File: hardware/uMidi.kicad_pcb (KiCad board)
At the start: 2 copper layers, 66 x 40.6 mm, 65 parts, among them CON1 USB-MINI-B, IC1 ATXMEGA128A4U-M, IC2 74LS14, IC3 LT1129CST-3.3, IC4 6N138, P1 MIDI In, P2 MIDI Thru, P3 MIDI T/O, P4 MIDI Out, P5 5..12 V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

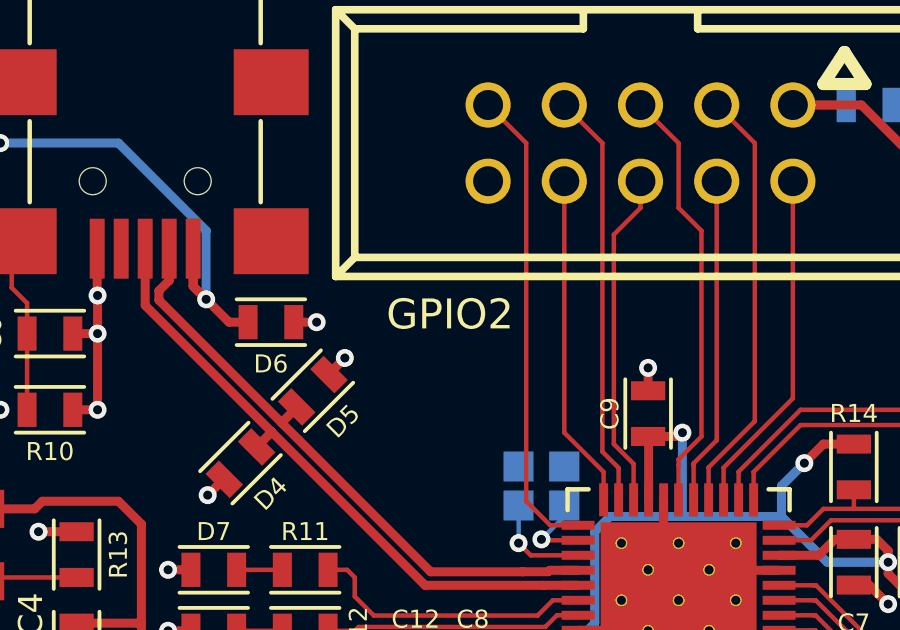
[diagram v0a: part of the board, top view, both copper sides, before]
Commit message: Fix GPIO3 value and silkscreen text
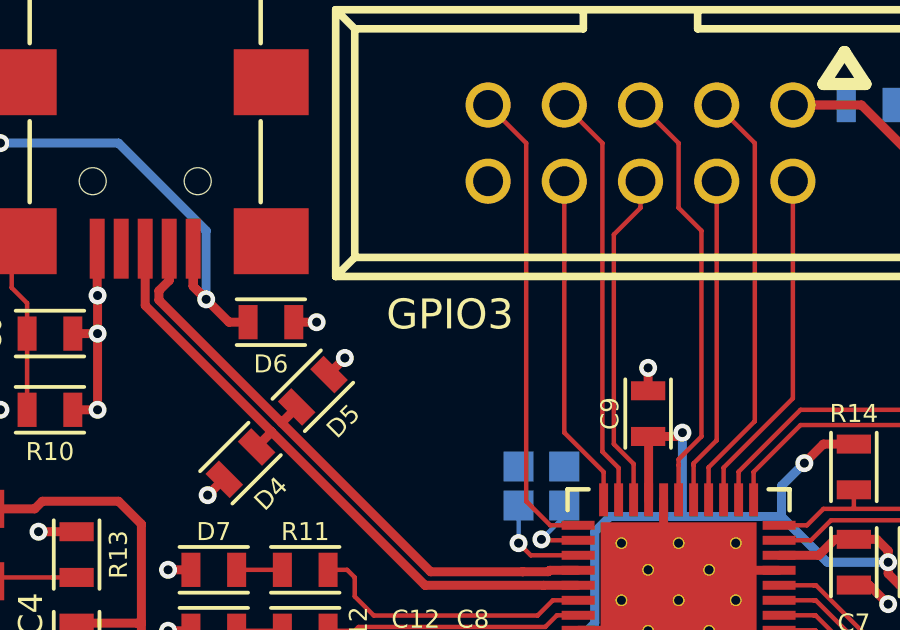
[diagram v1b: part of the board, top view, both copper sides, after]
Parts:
- P9: value GPIO2 -> GPIO3
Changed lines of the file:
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@@
     (links 166)
     (no_connects 0)
-    (area 67.259999 117.955 133.400001 166.2406)
+    (area 67.259999 123.139999 133.400001 163.880001)
     (thickness 1.6)
     (drawings 24)
@@
   (layers
     (0 F.Cu signal)
-    (31 B.Cu signal hide)
+    (31 B.Cu signal)
     (32 B.Adhes user)
     (33 F.Adhes user)
@@
       (linewidth 0.020000)
       (plotframeref false)
-      (viasonmask false)
+      (viasonmask true)
       (mode 1)
       (useauxorigin false)
@@
       (padsonsilk false)
       (subtractmaskfromsilk false)
-      (outputformat 4)
+      (outputformat 1)
       (mirror false)
-      (drillshape 2)
+      (drillshape 0)
       (scaleselection 1)
       (outputdirectory plots/))
@@
       (effects (font (size 1.778 1.778) (thickness 0.0889)))
     )
-    (fp_text value GPIO2 (at 6.35 -5.715 180) (layer F.SilkS)
+    (fp_text value GPIO3 (at 6.35 -5.715 180) (layer F.SilkS)
       (effects (font (size 1 1) (thickness 0.2)))
     )

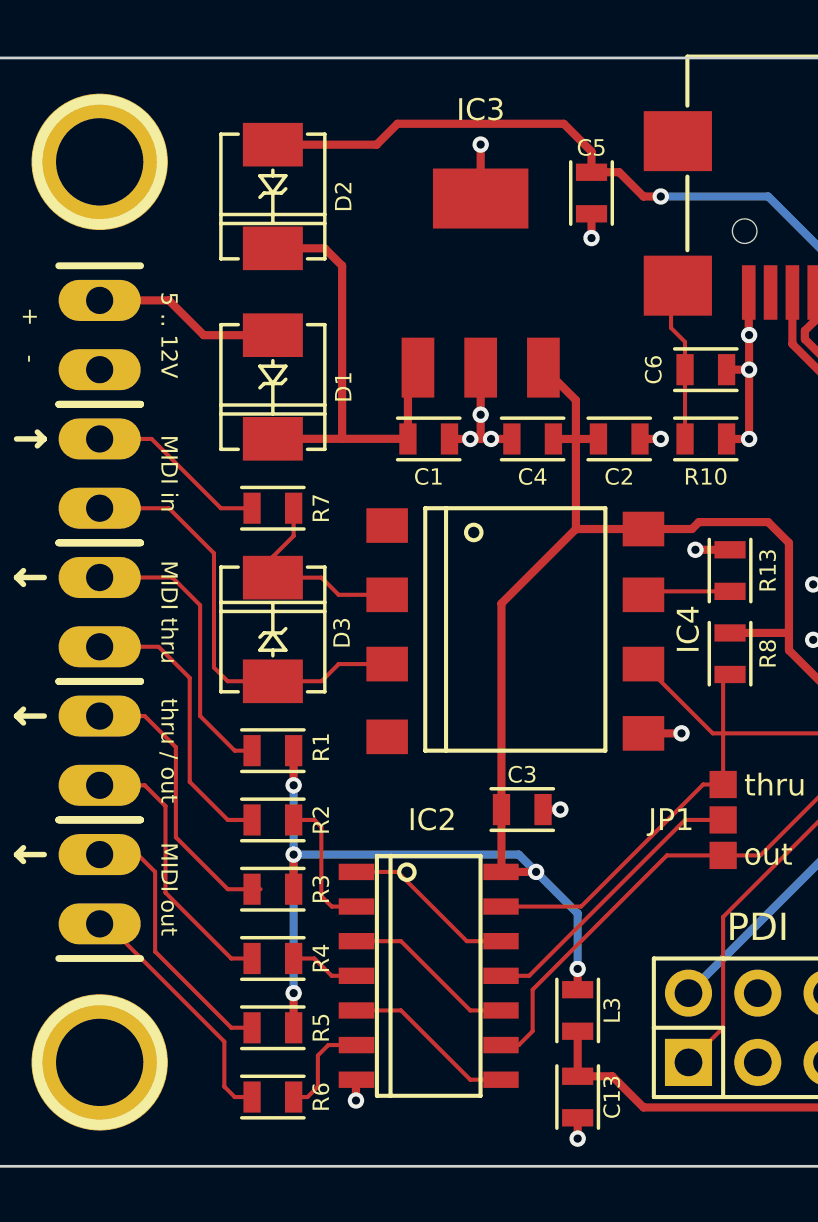
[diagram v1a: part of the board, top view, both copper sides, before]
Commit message: Revise silkscreen; Customize diode module
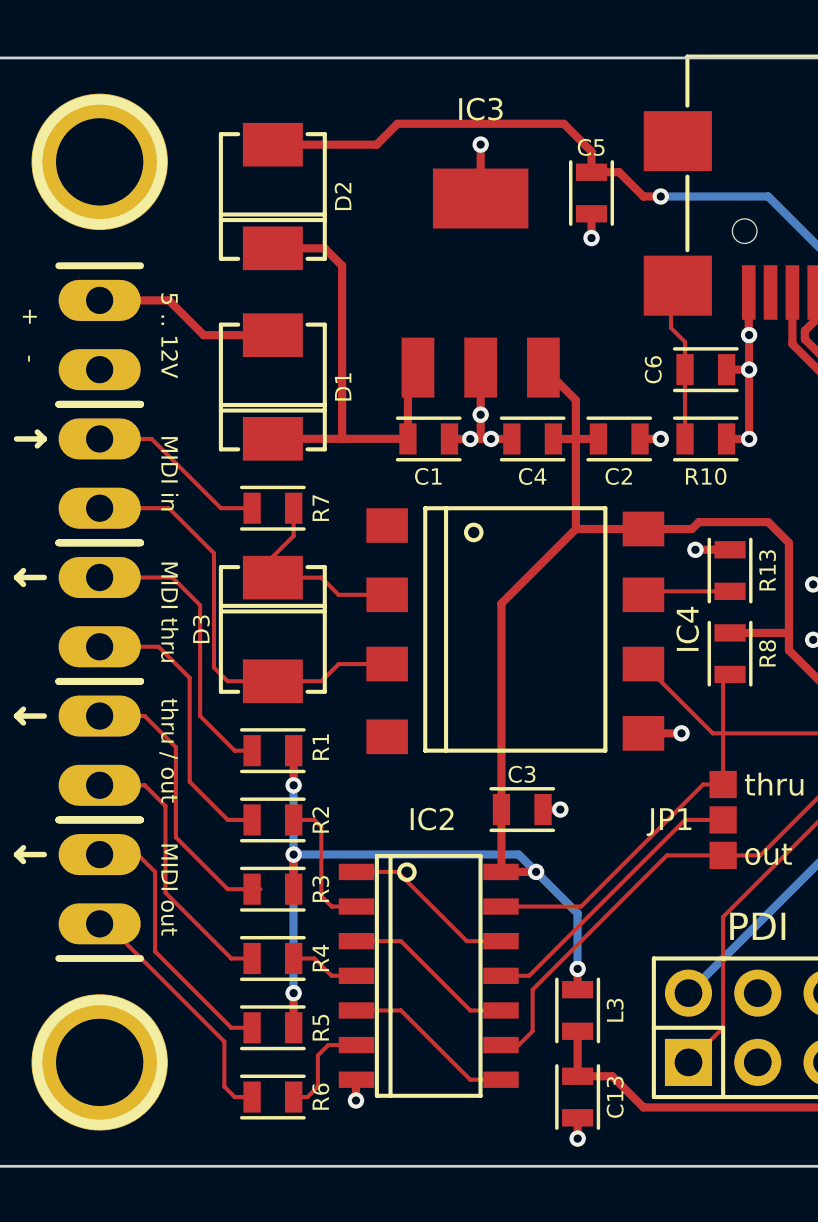
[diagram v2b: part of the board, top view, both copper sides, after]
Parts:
- D1, D2, D3: footprint SMD_Packages:DO-214-AC_SMA -> SMD:DO-214-AC_SMA

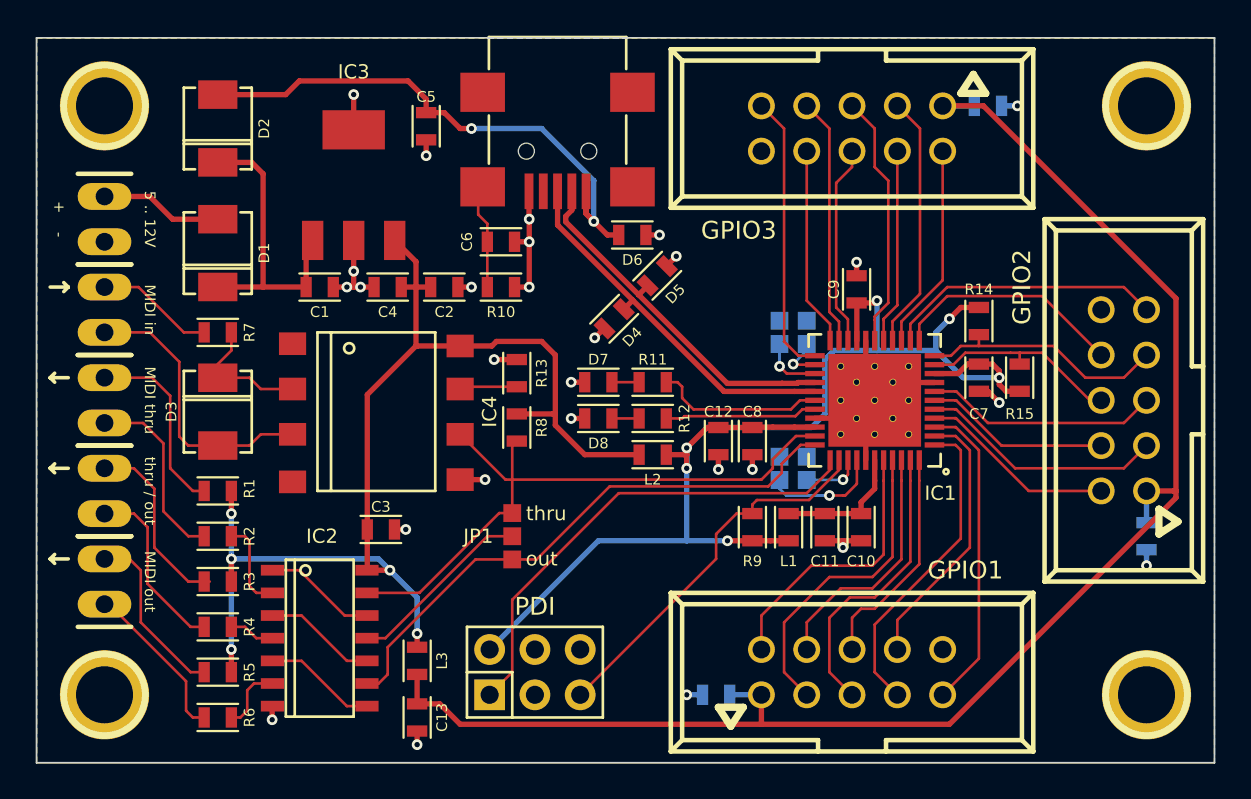
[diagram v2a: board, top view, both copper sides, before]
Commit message: Add copyright notice and project name
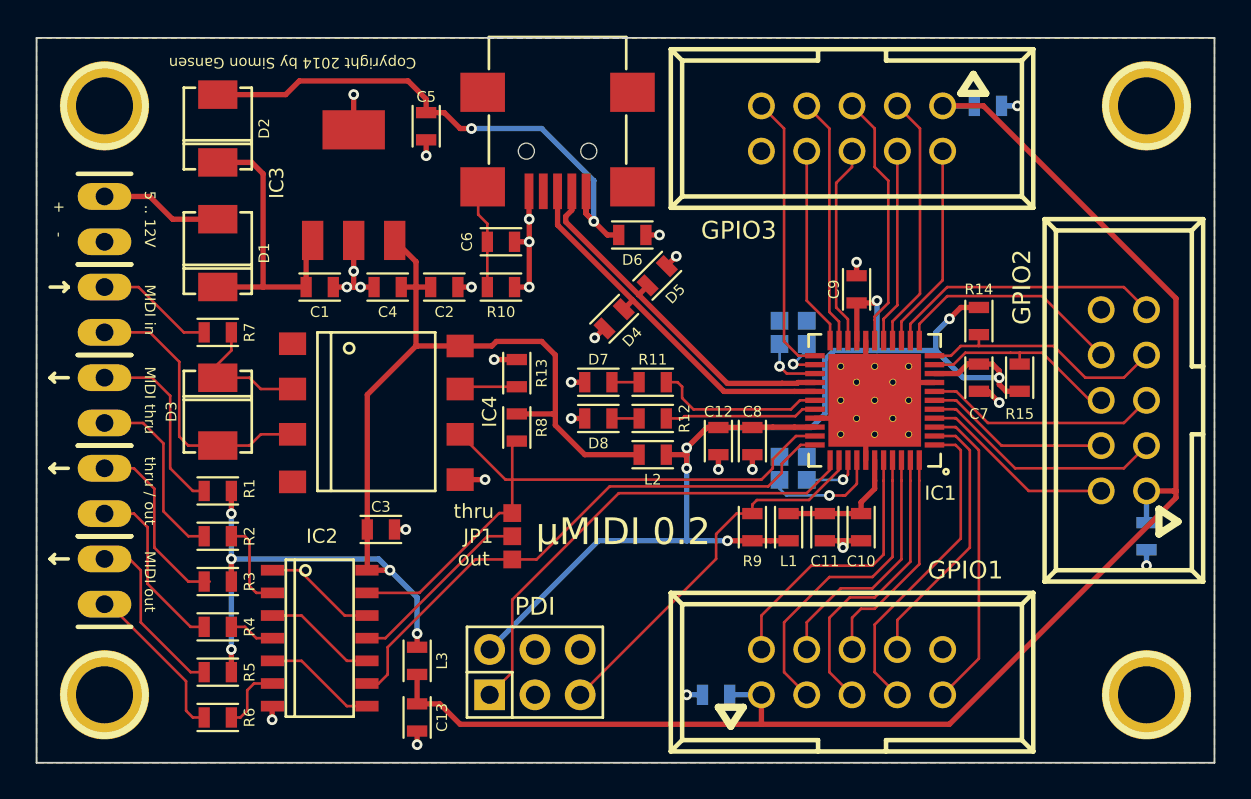
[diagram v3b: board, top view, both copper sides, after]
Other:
- board text added: "Copyright 2014 by Simon Gansen"
- board text added: "µMIDI 0.2"
